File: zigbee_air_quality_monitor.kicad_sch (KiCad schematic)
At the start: 31 parts, among them J1 USB_C_Receptacle_USB2.0, J2 QWIIC, J3 Conn_02x02_Odd_Even, SW1 PAIR_BTN, SW2 USER_BTN, U1 USBLC6-2SC6, U2 BT840, U3 XC6206P332MR, U4 SCD41-D-R2

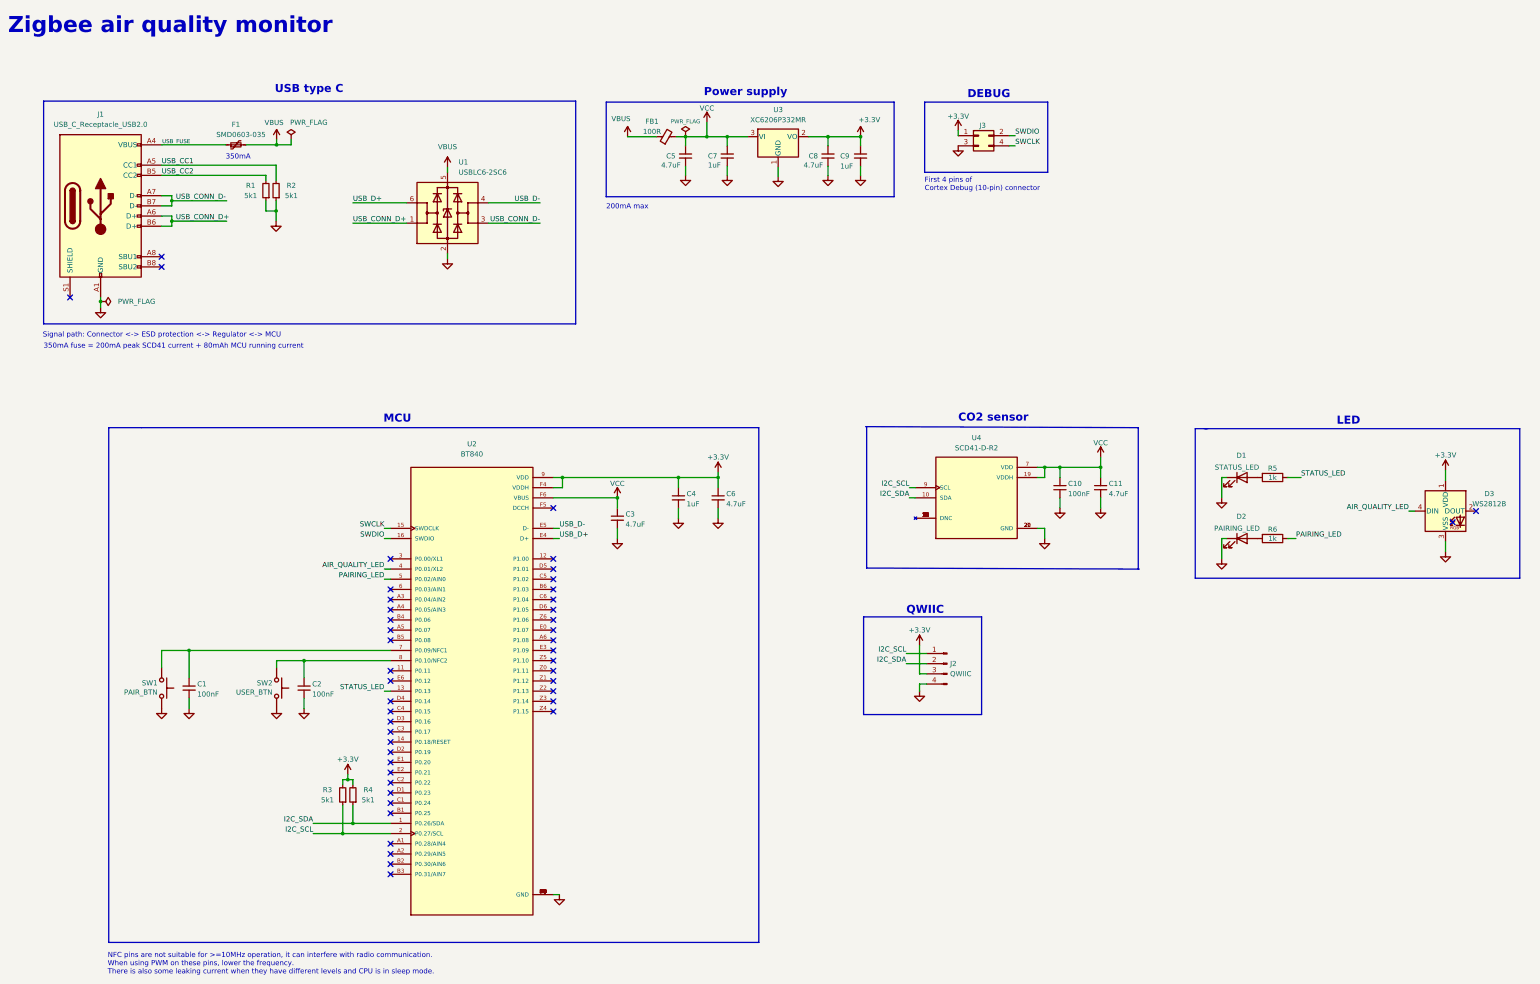
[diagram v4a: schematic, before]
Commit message: Added level translator for SCD40
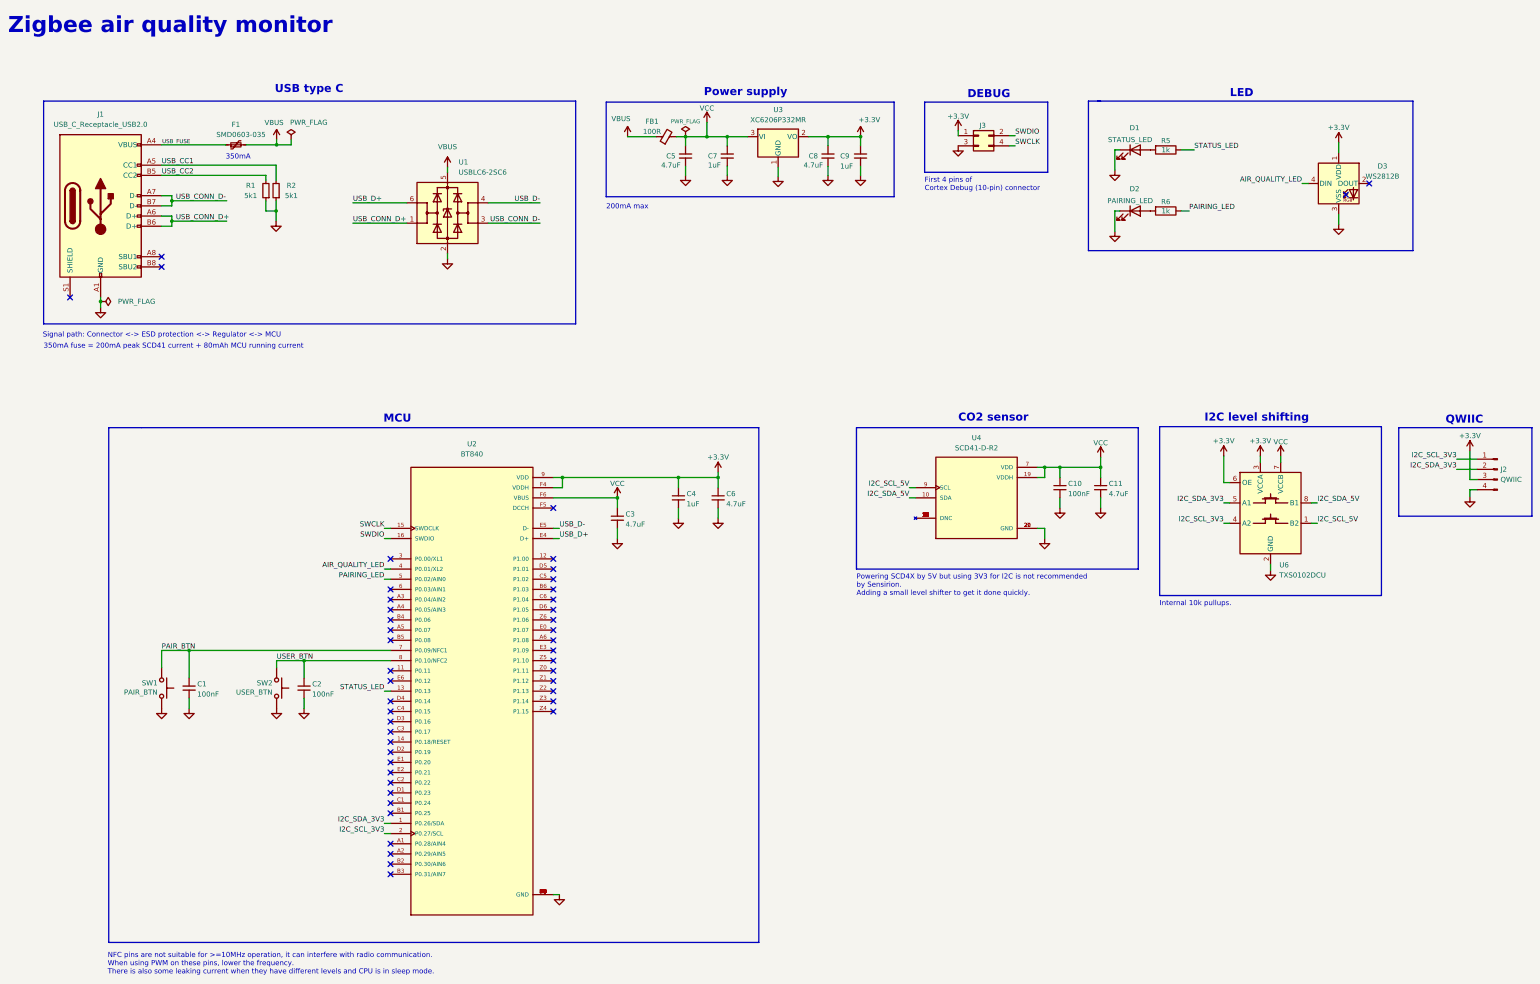
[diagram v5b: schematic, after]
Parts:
- removed R3, R4: 5k1, Resistor_SMD:R_0603_1608Metric, symbol Device:R_Small
- added U6: TXS0102DCU, Package_SO:VSSOP-8_2.3x2mm_P0.5mm, symbol Logic_LevelTranslator:TXS0102DCU
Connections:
- net +3.3V: now also U6.3 (VCCA), U6.6 (OE)
- net GND: now also U6.2 (GND)
- net VCC: now also U6.7 (VCCB)
- net PAIR_BTN: now reaches C1.1, SW1.1, U2.7 (P0.09/NFC1)
- net USER_BTN: now reaches C2.1, SW2.1, U2.8 (P0.10/NFC2)
- net I2C_SCL renamed I2C_SCL_3V3
- net I2C_SCL_3V3: now also U6.4 (A2); no longer U4.9 (SCL)
- net I2C_SDA renamed I2C_SDA_3V3
- net I2C_SDA_3V3: now also U6.5 (A1); no longer U4.10 (SDA)
- new net I2C_SCL_5V: U4.9 (SCL), U6.1 (B2)
- new net I2C_SDA_5V: U4.10 (SDA), U6.8 (B1)
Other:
- note added: "I2C level shifting"
- note added: "Internal 10k pullups."
- note added: "Powering SCD4X by 5V but using 3V3 for I2C is not recommended by Sensirion. Adding a small level shifter to get it done quickly."
- moved on the sheet: D1, D2, D3, J2, R5, R6
